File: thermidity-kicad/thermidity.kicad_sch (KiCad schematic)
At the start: 18 parts, among them J1 Battery, J2 Display, J3 ISP, U1 MCP1501-30, U2 ATmega328P, U3 TMP36, U4 HIH-5030

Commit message: improve PCB
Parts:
- renumbered C6 to C5, C5 to C6, R3 to R2, R2 to R3
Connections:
- net at U2.23 (PC0): no longer U3.2 (VOUT)
- net at R4.1, U4.2 (OUT): now also U2.26 (PC3); no longer U2.24 (PC1)
- net at R2.1, R3.2: now also U2.24 (PC1); no longer U2.25 (PC2)
- new net: U2.25 (PC2), U3.2 (VOUT)
- no-connect marks 17 -> 16
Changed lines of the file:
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@@
   (no_connect (at 130.81 73.66))
   (no_connect (at 161.29 83.82))
-  (no_connect (at 161.29 96.52))
   (no_connect (at 130.81 71.12))
   (no_connect (at 161.29 109.22))
@@
     (stroke (width 0) (type default) (color 0 0 0 0))
   )
-  (wire (pts (xy 163.83 135.89) (xy 163.83 91.44))
+  (wire (pts (xy 163.83 135.89) (xy 163.83 96.52))
     (stroke (width 0) (type default) (color 0 0 0 0))
   )
@@
     (stroke (width 0) (type default) (color 0 0 0 0))
   )
-  (wire (pts (xy 166.37 49.53) (xy 176.53 49.53))
+  (wire (pts (xy 163.83 49.53) (xy 176.53 49.53))
     (stroke (width 0) (type default) (color 0 0 0 0))
   )
@@
     (stroke (width 0) (type default) (color 0 0 0 0))
   )
-  (wire (pts (xy 163.83 43.18) (xy 199.39 43.18))
-    (stroke (width 0) (type default) (color 0 0 0 0))
-  )
-  (wire (pts (xy 166.37 93.98) (xy 166.37 49.53))
+  (wire (pts (xy 166.37 43.18) (xy 199.39 43.18))
     (stroke (width 0) (type default) (color 0 0 0 0))
   )
@@
     (stroke (width 0) (type default) (color 0 0 0 0))
   )
-  (wire (pts (xy 161.29 88.9) (xy 163.83 88.9))
-    (stroke (width 0) (type default) (color 0 0 0 0))
-  )
   (wire (pts (xy 199.39 137.16) (xy 203.2 137.16))
     (stroke (width 0) (type default) (color 0 0 0 0))
@@
     (stroke (width 0) (type default) (color 0 0 0 0))
   )
+  (wire (pts (xy 163.83 91.44) (xy 161.29 91.44))
+    (stroke (width 0) (type default) (color 0 0 0 0))
+  )
   (wire (pts (xy 93.98 71.12) (xy 83.82 71.12))
     (stroke (width 0) (type default) (color 0 0 0 0))
@@
     (stroke (width 0) (type default) (color 0 0 0 0))
   )
-  (wire (pts (xy 163.83 91.44) (xy 161.29 91.44))
-    (stroke (width 0) (type default) (color 0 0 0 0))
-  )
-  (wire (pts (xy 161.29 93.98) (xy 166.37 93.98))
-    (stroke (width 0) (type default) (color 0 0 0 0))
-  )
   (wire (pts (xy 190.5 81.28) (xy 203.2 81.28))
     (stroke (width 0) (type default) (color 0 0 0 0))
@@
     (stroke (width 0) (type default) (color 0 0 0 0))
   )
+  (wire (pts (xy 163.83 49.53) (xy 163.83 91.44))
+    (stroke (width 0) (type default) (color 0 0 0 0))
+  )
+  (wire (pts (xy 161.29 96.52) (xy 163.83 96.52))
+    (stroke (width 0) (type default) (color 0 0 0 0))
+  )
   (wire (pts (xy 115.57 132.08) (xy 115.57 143.51))
     (stroke (width 0) (type default) (color 0 0 0 0))
@@
     (stroke (width 0) (type default) (color 0 0 0 0))
   )
-  (wire (pts (xy 163.83 88.9) (xy 163.83 43.18))
-    (stroke (width 0) (type default) (color 0 0 0 0))
-  )
   (wire (pts (xy 128.27 81.28) (xy 128.27 66.04))
     (stroke (width 0) (type default) (color 0 0 0 0))
@@
     (stroke (width 0) (type default) (color 0 0 0 0))
   )
+  (wire (pts (xy 166.37 43.18) (xy 166.37 93.98))
+    (stroke (width 0) (type default) (color 0 0 0 0))
+  )
   (wire (pts (xy 176.53 59.69) (xy 176.53 62.23))
     (stroke (width 0) (type default) (color 0 0 0 0))
@@
     (stroke (width 0) (type default) (color 0 0 0 0))
   )
+  (wire (pts (xy 166.37 93.98) (xy 161.29 93.98))
+    (stroke (width 0) (type default) (color 0 0 0 0))
+  )
   (wire (pts (xy 130.81 33.02) (xy 93.98 33.02))
     (stroke (width 0) (type default) (color 0 0 0 0))
@@
   (symbol (lib_id "Device:C") (at 187.96 43.18 0) (unit 1)
     (in_bom yes) (on_board yes) (fields_autoplaced)
-    (property "Reference" "C6" (id 0) (at 191.77 41.9099 0)
+    (property "Reference" "C5" (id 0) (at 191.77 41.9099 0)
       (effects (font (size 1.27 1.27)) (justify left))
     )
@@
   (symbol (lib_id "Device:C") (at 120.65 43.18 90) (unit 1)
     (in_bom yes) (on_board yes) (fields_autoplaced)
-    (property "Reference" "C5" (id 0) (at 120.65 35.56 90))
+    (property "Reference" "C6" (id 0) (at 120.65 35.56 90))
     (property "Value" "100nF" (id 1) (at 120.65 38.1 90))
     (property "Footprint" "Capacitor_SMD:C_1206_3216Metric_Pad1.33x1.80mm_HandSolder" (id 2) (at 124.46 42.2148 0)
@@
   (symbol (lib_id "Device:R") (at 176.53 55.88 0) (unit 1)
     (in_bom yes) (on_board yes) (fields_autoplaced)
-    (property "Reference" "R3" (id 0) (at 179.07 54.6099 0)
+    (property "Reference" "R2" (id 0) (at 179.07 54.6099 0)
       (effects (font (size 1.27 1.27)) (justify left))
     )
@@
   (symbol (lib_id "Device:R") (at 176.53 43.18 0) (unit 1)
     (in_bom yes) (on_board yes) (fields_autoplaced)
-    (property "Reference" "R2" (id 0) (at 179.07 41.9099 0)
+    (property "Reference" "R3" (id 0) (at 179.07 41.9099 0)
       (effects (font (size 1.27 1.27)) (justify left))
     )
@@
       (reference "C4") (unit 1) (value "2.2uF") (footprint "Capacitor_SMD:C_1206_3216Metric_Pad1.33x1.80mm_HandSolder")
     )
+    (path "/0178a398-4cac-462d-a5f8-54e853b1fa89"
+      (reference "C5") (unit 1) (value "100nF") (footprint "Capacitor_SMD:C_1206_3216Metric_Pad1.33x1.80mm_HandSolder")
+    )
     (path "/8e459bfb-75fb-4c36-90af-73c840018779"
-      (reference "C5") (unit 1) (value "100nF") (footprint "Capacitor_SMD:C_1206_3216Metric_Pad1.33x1.80mm_HandSolder")
-    )
-    (path "/0178a398-4cac-462d-a5f8-54e853b1fa89"
       (reference "C6") (unit 1) (value "100nF") (footprint "Capacitor_SMD:C_1206_3216Metric_Pad1.33x1.80mm_HandSolder")
     )
@@
       (reference "R1") (unit 1) (value "50") (footprint "Resistor_SMD:R_0805_2012Metric_Pad1.20x1.40mm_HandSolder")
     )
+    (path "/d690645f-ce9c-4e4e-9a40-30e90181925c"
+      (reference "R2") (unit 1) (value "1M") (footprint "Resistor_SMD:R_0805_2012Metric_Pad1.20x1.40mm_HandSolder")
+    )
     (path "/f5367a98-6a53-432b-8730-086e1bb8663c"
-      (reference "R2") (unit 1) (value "1M") (footprint "Resistor_SMD:R_0805_2012Metric_Pad1.20x1.40mm_HandSolder")
-    )
-    (path "/d690645f-ce9c-4e4e-9a40-30e90181925c"
       (reference "R3") (unit 1) (value "1M") (footprint "Resistor_SMD:R_0805_2012Metric_Pad1.20x1.40mm_HandSolder")
     )

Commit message: use print instead of SMD for JST connector
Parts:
- J1: footprint Connector_JST:JST_PH_S2B-PH-SM4-TB_1x02-1MP_P2.00mm_Horizontal -> Connector_JST:JST_PH_S2B-PH-K_1x02_P2.00mm_Horizontal
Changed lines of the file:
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@@
       (effects (font (size 1.27 1.27)) (justify left))
     )
-    (property "Footprint" "Connector_JST:JST_PH_S2B-PH-SM4-TB_1x02-1MP_P2.00mm_Horizontal" (id 2) (at 208.28 137.16 0)
+    (property "Footprint" "Connector_JST:JST_PH_S2B-PH-K_1x02_P2.00mm_Horizontal" (id 2) (at 208.28 137.16 0)
       (effects (font (size 1.27 1.27)) hide)
     )
@@
     )
     (path "/346b2658-5c55-45ae-8c48-4ce2f357fb5f"
-      (reference "J1") (unit 1) (value "Battery") (footprint "Connector_JST:JST_PH_S2B-PH-SM4-TB_1x02-1MP_P2.00mm_Horizontal")
+      (reference "J1") (unit 1) (value "Battery") (footprint "Connector_JST:JST_PH_S2B-PH-K_1x02_P2.00mm_Horizontal")
     )
     (path "/0e5b05aa-5b3c-4c4e-aeb5-7fb463ba565b"

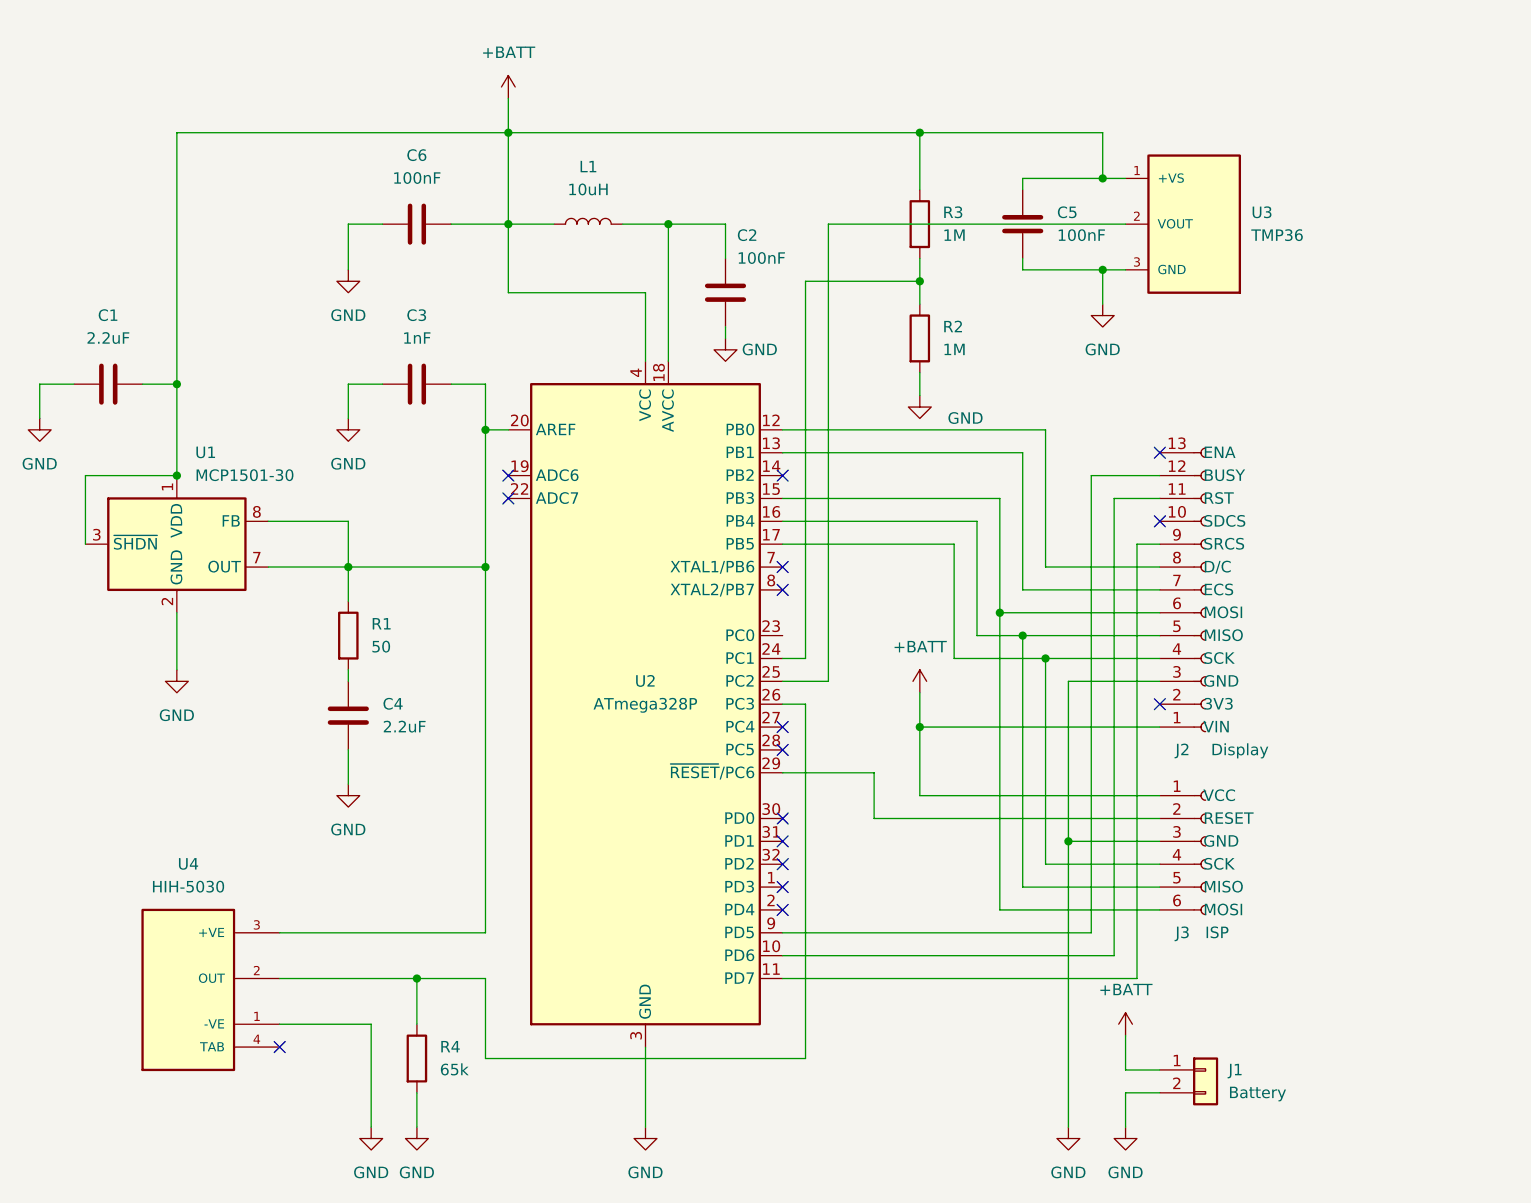
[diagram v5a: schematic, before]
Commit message: power off vref during idle time reducing consumption from 400uA to 43uA
- power off vref including humidity sensor
- add serial resistor to reduce charge current
- fix pin initialization
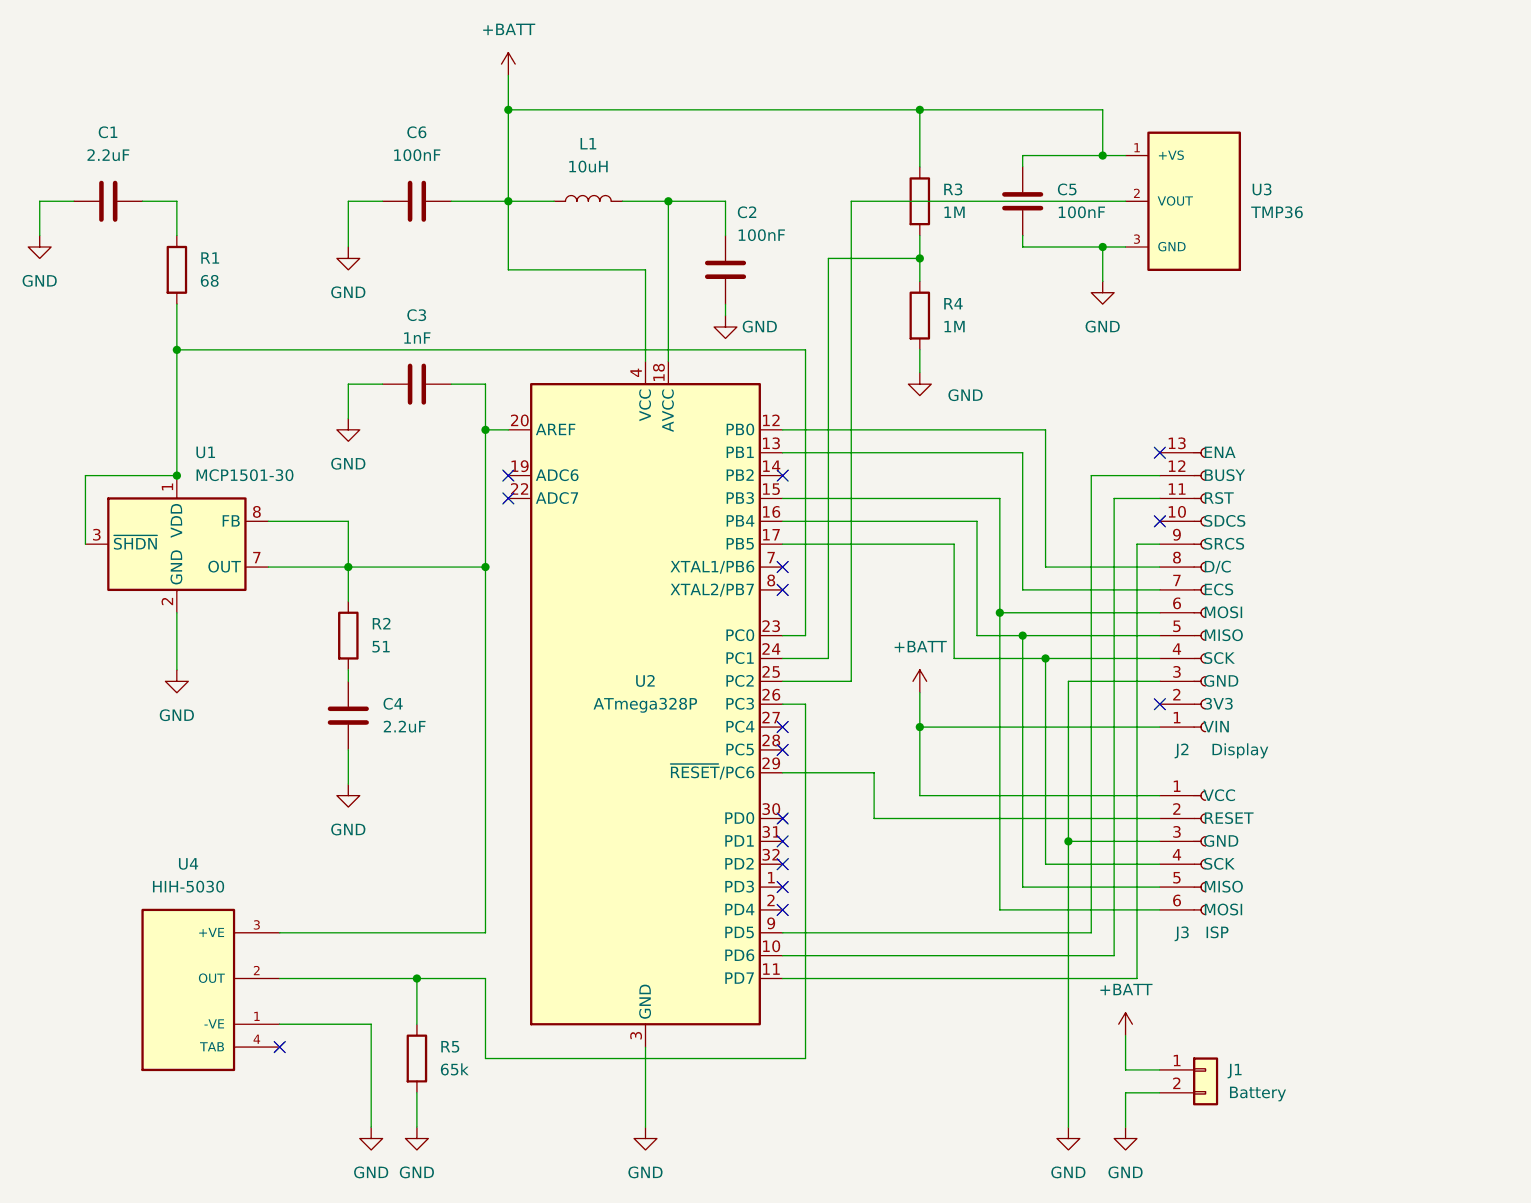
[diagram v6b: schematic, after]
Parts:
- added R1: 68, Resistor_SMD:R_0805_2012Metric_Pad1.20x1.40mm_HandSolder, symbol Device:R
- R2: renamed from R1; value 50 -> 51
- renumbered R2 to R4, R4 to R5
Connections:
- net +BATT: no longer C1.2, U1.1 (VDD), U1.3 (~{SHDN})
- net at U2.23 (PC0): now also U1.1 (VDD), U1.3 (~{SHDN}), R1.2
- new net: C1.2, R1.1
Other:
- moved on the sheet: C1, C2, C5, C6, L1, R3, R4, U3

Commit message: ratiometric measurement of humidity (#16)
- removed voltage refererence
- TMP36 to be replaced by thermistor (currently dependent on battery voltage)
- battery voltage measurement should use internal 1.1 Vref (does not need to be accurate)
- update schematic and README
- update PCB
- measure battery voltage using internal 1.1V reference
- lower "low battery" limit to 3V which is the minimum for the display
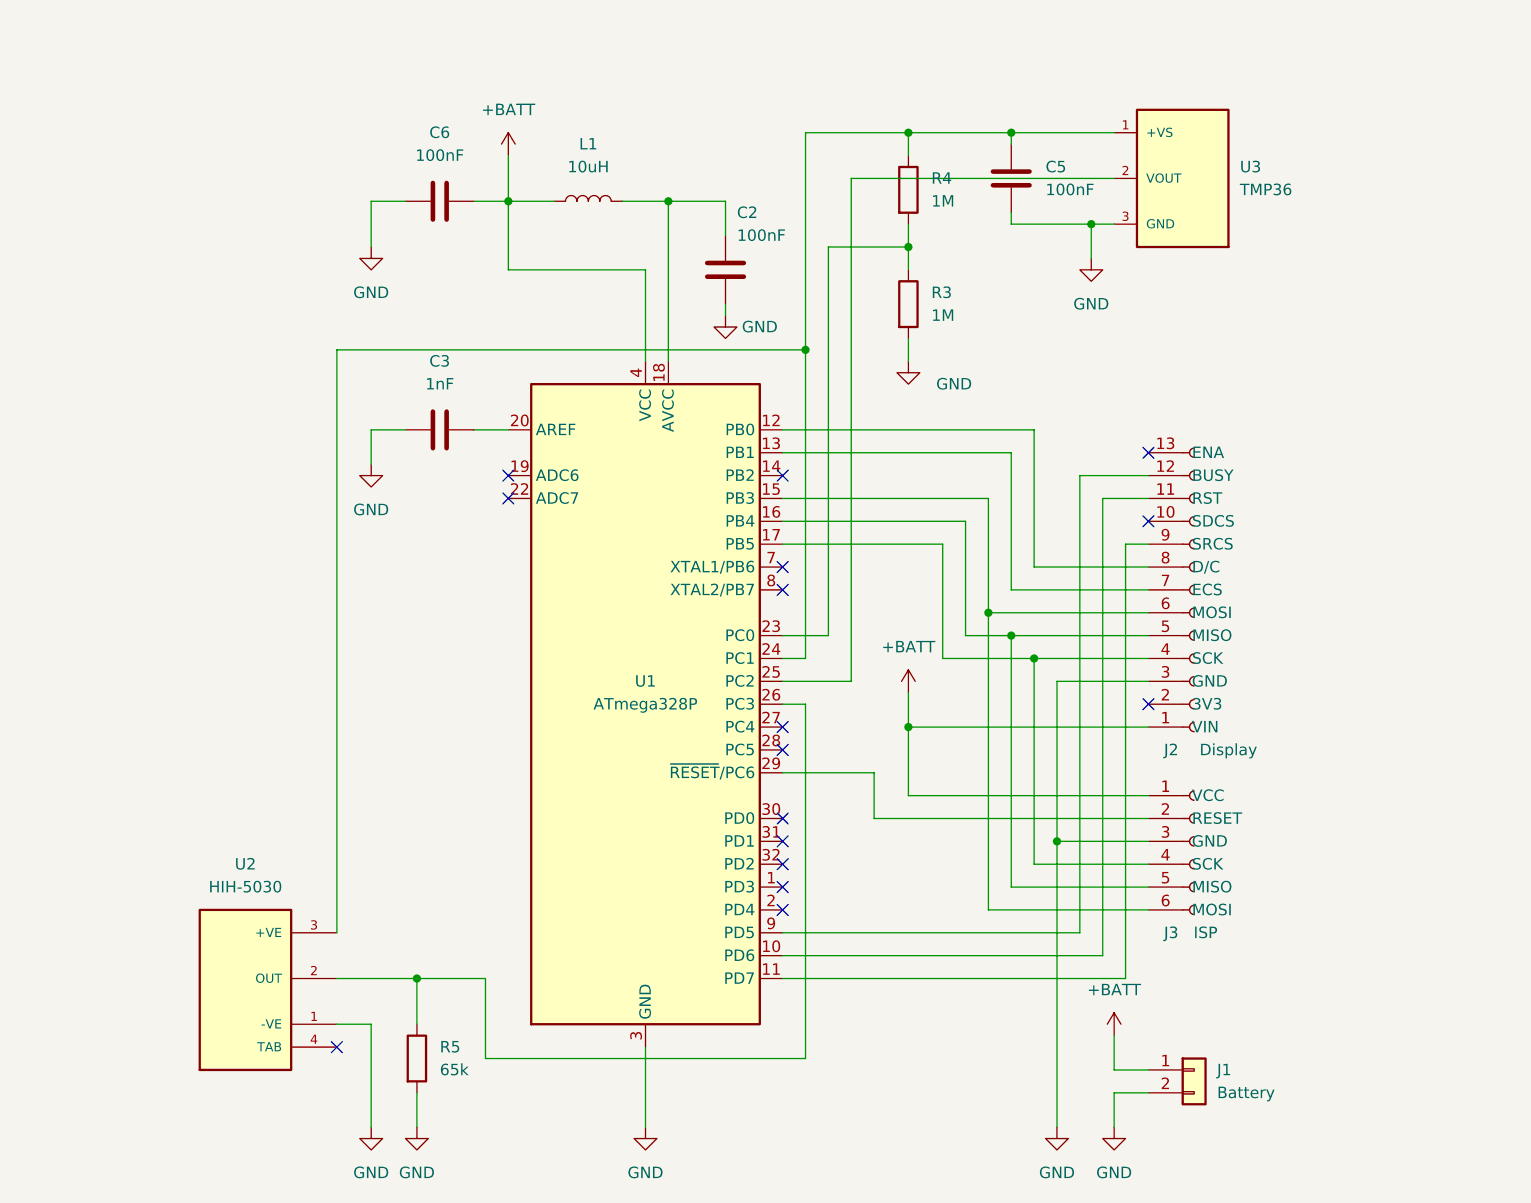
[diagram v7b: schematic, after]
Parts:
- removed C1, C4: 2.2uF, Capacitor_SMD:C_1206_3216Metric_Pad1.33x1.80mm_HandSolder, symbol Device:C
- removed R1: 68, Resistor_SMD:R_0805_2012Metric_Pad1.20x1.40mm_HandSolder, symbol Device:R
- removed R2: 51, Resistor_SMD:R_0805_2012Metric_Pad1.20x1.40mm_HandSolder, symbol Device:R
- removed U1: MCP1501-30, Package_SO:SOIC-8_3.9x4.9mm_P1.27mm, symbol Reference_Voltage:MCP1501-30xSN
- renumbered R4 to R3, R3 to R4, U2 to U1, U4 to U2
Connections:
- net +BATT: no longer C5.1, R4.1, U3.1 (+VS)
- net at C3.2, U1.20 (AREF): no longer U2.3 (+VE)
- net at U1.23 (PC0): now also R3.1, R4.2
- new net: C5.1, R4.1, U1.24 (PC1), U2.3 (+VE), U3.1 (+VS)
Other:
- moved on the sheet: C3, C5, C6, J1, J2, J3, R3, R4, U2, U3
